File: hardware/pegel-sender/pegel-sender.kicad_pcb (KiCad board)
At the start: 2 copper layers, 100 x 70 mm, 125 parts, among them J1 SOLAR, J2 AKKU 3,2V, J3 SONDE V+ V- A B, J4 NTC extern, J5 XIAO D0-D6, J6 XIAO 5V-D7, J7 12V, Q1 AOD4189, Q10 2N7002, Q11 2N7002, Q2 FS8205A, Q3 FS8205A, Q4 AO3401A, Q5 2N7002, Q6 2N7002, Q7 SI2318CDS, Q8 2N7002, Q9 AO3401A, U1 CN3795, U10 TLV3401, U2 INA226, U3 HY2112-CB, U4 TPS63900, U5 TPS61040, U6 SC16IS740, U7 MAX3485, U8 TLV3402, U9 LM66100, Y1 14.7456MHz

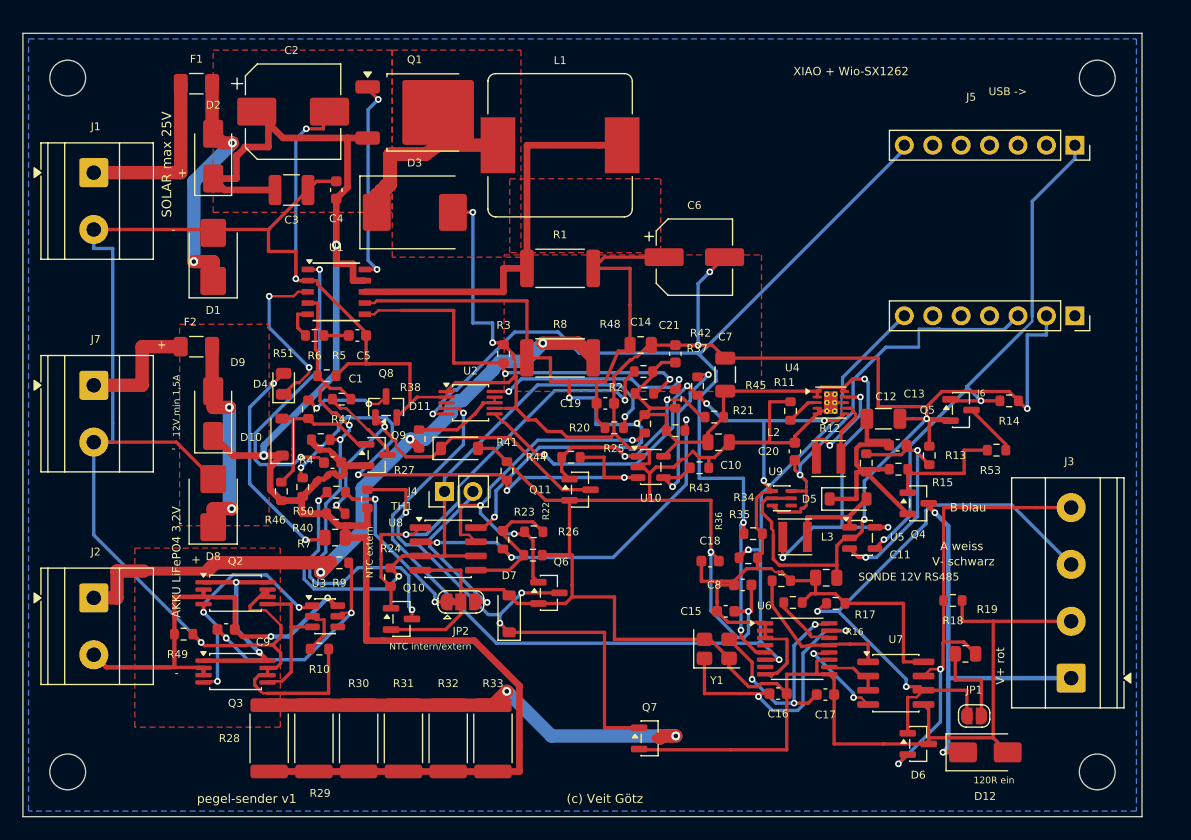
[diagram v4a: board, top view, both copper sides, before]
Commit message: hardware: circuit simulation, component stress and trace check with fixes
SPICE suite (verify/) built from design.py: 19 operating cases, sweeps,
long-term run, IPC-2221 trace check; firmware host tests with emulated
probe, SC16IS740 and INA226.

Fixes found by it: D14 blocks battery backfeed into the heater, MPPT
detection on DC_F with hysteresis, more input capacitance (C4 1210, C22),
new frost thresholds, LM2735 boost for 200 mA probe peaks, battery-low
hysteresis in firmware. Board: fixed 1.2 mm tracks L1-R1-R8, D3 and
protection FET ground vias, B.Cu keepout under the FETs.
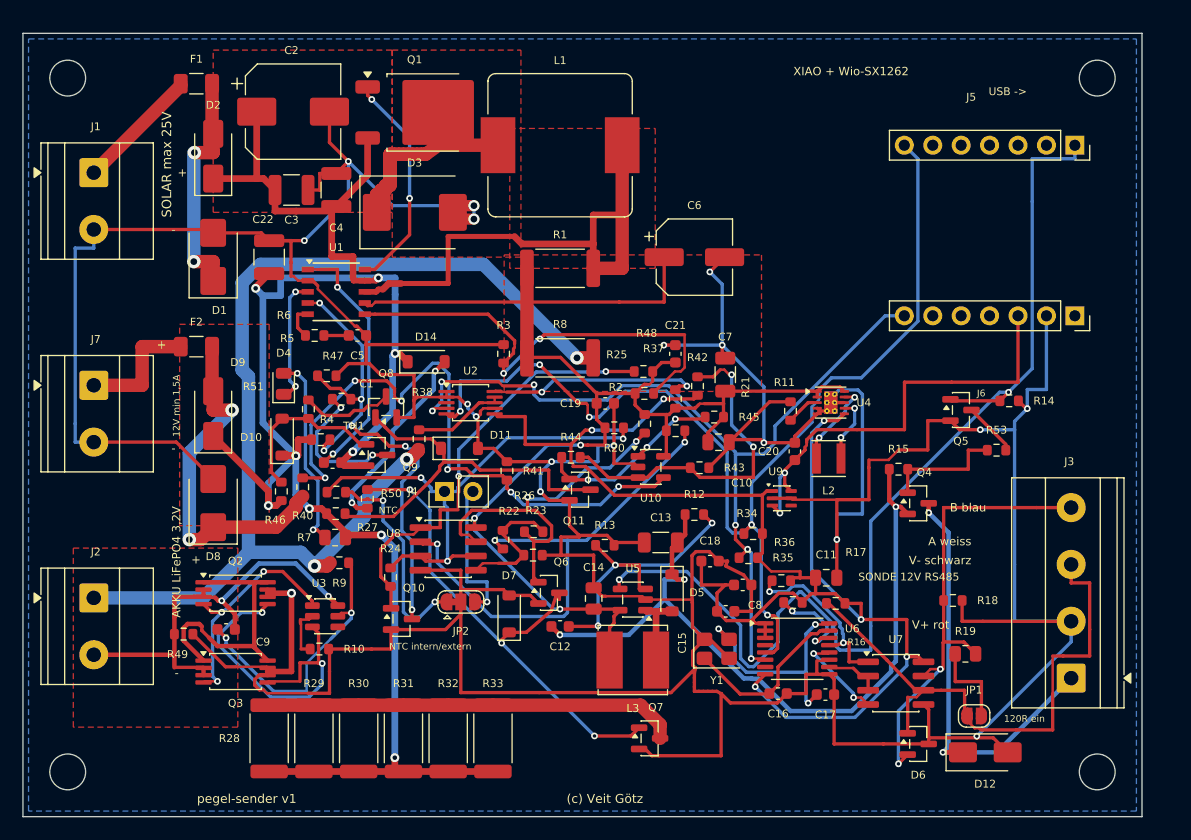
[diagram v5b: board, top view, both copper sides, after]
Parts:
- added C22: 10uF 50V, Capacitor_SMD:C_1210_3225Metric, F.Cu at (72.0, 70.0)
- added D14: 5V6, Diode_SMD:D_SOD-123, F.Cu at (86.0, 79.3)
- C1: value 100nF -> 100nF 50V
- C10: value 10uF -> 10uF 10V
- C11: value 22uF -> 22uF 6.3V
- C12: value 22pF -> 22pF 50V
- C13: value 4.7uF -> 10uF 25V
- C14: value 4.7uF -> 22uF 10V
- C15, C18, C19, C21, C8, C9: value 100nF -> 100nF 16V
- C16, C17: value 27pF -> 27pF 50V
- C20: value 1uF -> 1uF 10V
- C3: value 10uF -> 10uF 50V
- C4: value 100nF -> 10uF 50V; footprint Capacitor_SMD:C_0603_1608Metric -> Capacitor_SMD:C_1210_3225Metric
- C5: value 220nF -> 220nF 16V
- C7: value 10uF -> 10uF 16V
- J4: value NTC extern -> NTC
- L3: value 10uH -> 4.7uH; footprint Inductor_SMD:L_Taiyo-Yuden_NR-30xx -> Inductor_SMD:L_Bourns_SRN6045TA
- R1: value 40m -> 40m 2W
- R13: value 91k -> 93.1k
- R21: value 470k -> 499k
- R22: value 28.7k -> 53.6k
- R23: value 499k -> 453k
- R28, R29, R30, R31, R32, R33: value 390 -> 390 2W
- R40: value 470k -> 33k
- R41: value 68.1k -> 10k
- R8: value 10m -> 10m 2W
- U5: value TPS61040 -> LM2735
- moved C12 34.2 mm to (98.0, 103.0)
- moved R13 30.1 mm to (102.0, 95.8), turned to 0 degrees
- moved C14 23.0 mm to (101.0, 100.5), turned to 90 degrees
- moved C13 22.8 mm to (107.0, 95.5), turned to 180 degrees
- moved U5 21.2 mm to (104.5, 100.6), turned to 180 degrees
- moved L3 18.2 mm to (104.5, 106.0)
- moved D5 17.8 mm to (108.0, 100.0), turned to -90 degrees
- moved R12 16.0 mm to (110.0, 93.0), turned to 0 degrees
- turned R1 to 180 degrees
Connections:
- R27 pad 1: VSOL -> HEAT_PU
- R40 pad 1: VSOL -> DC_F
- R40 pad 2: VSOL_DIV -> DC_DIV
- R41 pad 1: VSOL_DIV -> DC_DIV
- R44 pad 2: VSOL_DIV -> MPPT_REF
- U10 pad 3: VSOL_DIV -> MPPT_REF
- U10 pad 4: MPPT_REF -> DC_DIV
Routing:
- net DC_DIV: track 0.00 -> 55.2 mm, vias 0 -> 6
- net VSOL_DIV: track 49.7 -> 0.00 mm, vias 4 -> 0
- net SENS_EN: track 49.8 -> 97.4 mm
- net V12_RAW: track 24.2 -> 68.1 mm, vias 0 -> 3
- net BAT_P: track 62.2 -> 97.8 mm
- net +3V3: track 102.0 -> 135.1 mm, vias 5 -> 6
- net VSYS: track 153.1 -> 128.1 mm, vias 6 -> 3
- net HEAT_PU: track 0.00 -> 17.6 mm, vias 0 -> 2
- net PROT_OC: track 12.6 -> 30.1 mm, vias 0 -> 2
- net CHG_CSP: track 36.1 -> 52.4 mm
- net I2C_SDA: track 92.7 -> 77.4 mm, vias 3 -> 6
- net MPPT_REF: track 16.3 -> 30.4 mm
- net DC_F: track 19.4 -> 32.5 mm
- net T_NTC: track 57.8 -> 45.7 mm
- net T_REF0: track 34.9 -> 46.2 mm
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
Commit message: hardware: larger D1, Q9 and D12; room for the J3 labels
- D1 SMBJ26A -> SMBJ28A (90 % of Vwm at -25 °C open circuit, was 97 %;
  SMBJ30A would break down above the CN3795's 33 V)
- Q9 AO3401A -> Si2319CDS (40 V, ±20 V): Uds 62 %, Ugs 50 %
- D12 SMAJ15A -> SMAJ18A: 68 % at 12.3 V
- J3: Q4, R15, R18, R19 and D12 moved; "SONDE 12V RS485" vertical
  beside the pin texts, which now sit next to their pins
- B.Cu keepout under Q2/Q3 extended to the board edge so signal
  tracks cannot fence in the GND island
- pcb_check.py evaluates zone fills on all of a zone's layers
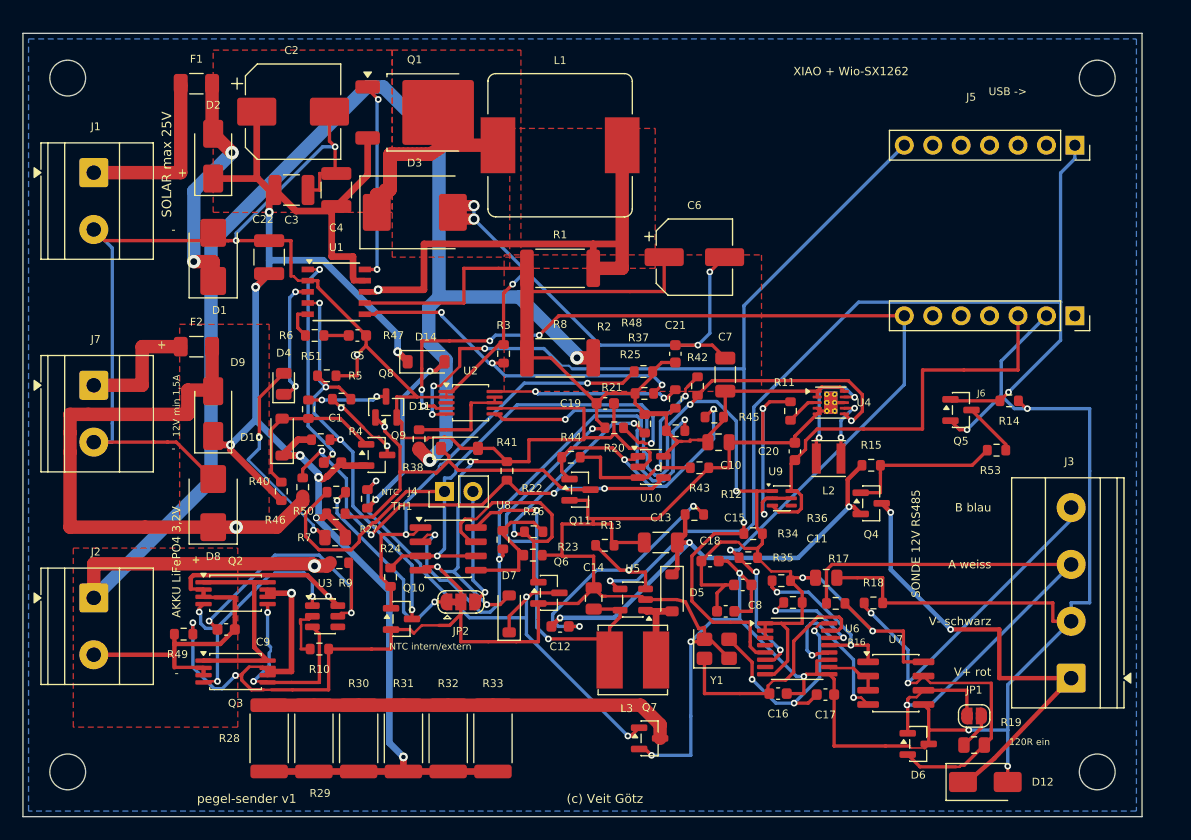
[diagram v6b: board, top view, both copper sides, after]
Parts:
- D1: value SMBJ26A -> SMBJ28A
- D12: value SMAJ15A -> SMAJ18A
- Q9: value AO3401A -> SI2319CDS
- moved R19 8.19 mm to (135.0, 113.6)
- moved R18 7.10 mm to (126.0, 100.9)
- moved Q4 4.20 mm to (125.8, 92.0)
- moved D12 2.65 mm to (136.0, 116.9)
- moved R15 2.46 mm to (125.8, 88.6)
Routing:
- net BAT_P: track 97.8 -> 136.3 mm
- net V12_RAW: track 68.1 -> 44.7 mm
- net GND: track 546.2 -> 564.9 mm, vias 18 -> 24
- net DC_F: track 32.5 -> 51.2 mm, vias 2 -> 1
- net T_NTC: track 45.7 -> 63.1 mm, vias 3 -> 2
- net I2C_SDA: track 77.4 -> 92.8 mm, vias 6 -> 7
- net DC_DIV: track 55.2 -> 41.7 mm, vias 6 -> 4
- net VSYS: track 128.1 -> 141.6 mm
- net +3V3: track 135.1 -> 123.6 mm
- net PROT_OC: track 30.1 -> 18.8 mm
- net CHG_FB: track 42.0 -> 31.6 mm, vias 2 -> 3
- net RS485_B: track 42.3 -> 52.4 mm
- net SENS_EN: track 97.4 -> 87.9 mm
- net MPPT_REF: track 30.4 -> 21.6 mm
- net VSOL: track 166.3 -> 157.8 mm, vias 9 -> 8
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
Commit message: hardware: cheapest JLCPCB build, basic/preferred parts only
All 45 SMD part types are JLCPCB basic or preferred (no loading fee);
inductors, terminals and XIAO sockets are through-hole for hand soldering.

- Charger: TPS5430 buck at 3.50 V; LM324 limits current to 2 A (shunt in
  the battery minus), holds the panel near 17 V (proportional loop, the
  integrator oscillated in weak light) and handles frost lock and heater.
  Single input for solar or 12 V supply, header jumper NETZTEIL.
- XIAO runs from the battery through a Schottky diode; no 3.3 V regulator,
  no INA226, no protection IC (firmware measures VDD, sleeps below 2.6 V).
- RS485: SP3485 on Serial1 with automatic direction, powered with the
  probe; no SC16IS740, no termination resistor.
- Probe 12 V from TPS61040 (30 mA).
- NTC and heater resistor at the battery via J4.
- New compact placement, 45 degree corners, wider traces and clearances,
  JLCPCB BOM/CPL export, user README, technical README for the board.
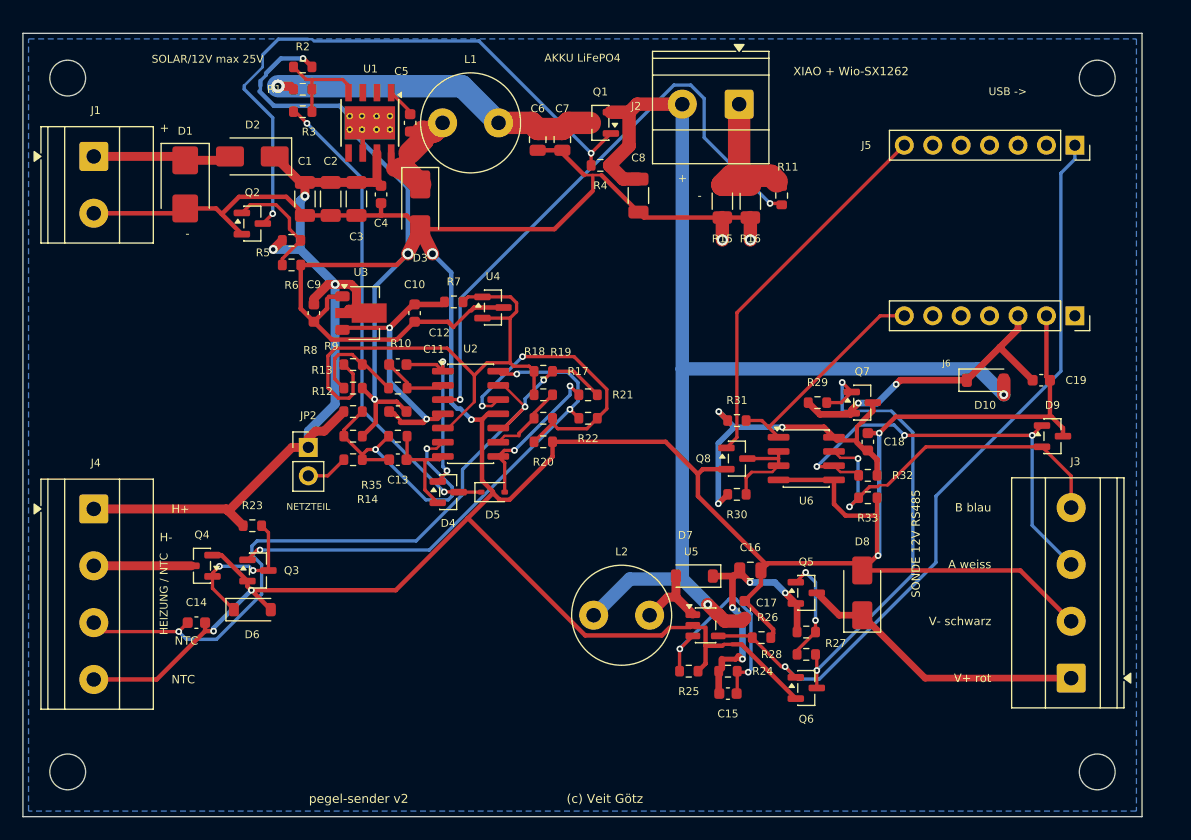
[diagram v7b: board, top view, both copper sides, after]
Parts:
- removed C20: 1uF 10V, Capacitor_SMD:C_0603_1608Metric
- removed C21: 100nF 16V, Capacitor_SMD:C_0603_1608Metric
- removed C22: 10uF 50V, Capacitor_SMD:C_1210_3225Metric
- removed D11: 10V, Diode_SMD:D_SOD-123
- removed D12: SMAJ18A, Diode_SMD:D_SMA
- removed D14: 5V6, Diode_SMD:D_SOD-123
- removed F1, F2: 2A, Fuse:Fuse_1206_3216Metric
- removed J7: 12V, TerminalBlock_Phoenix:TerminalBlock_Phoenix_MKDS-1,5-2-5.08_1x02_P5.08mm_Horizontal
- removed JP1: 120R ein, Jumper:SolderJumper-2_P1.3mm_Open_RoundedPad1.0x1.5mm
- removed L3: 4.7uH, Inductor_SMD:L_Bourns_SRN6045TA
- removed Q10, Q11: 2N7002, Package_TO_SOT_SMD:SOT-23
- removed Q9: SI2319CDS, Package_TO_SOT_SMD:SOT-23
- removed R34: 4.7k, Resistor_SMD:R_0603_1608Metric
- removed R36, R41, R51: 10k, Resistor_SMD:R_0603_1608Metric
- removed R37, R38: 10, Resistor_SMD:R_0603_1608Metric
- removed R40: 33k, Resistor_SMD:R_0603_1608Metric
- removed R42: 976k, Resistor_SMD:R_0603_1608Metric
- removed R43, R44, R45, R48, R50: 1M, Resistor_SMD:R_0603_1608Metric
- removed R46, R49, R53: 100k, Resistor_SMD:R_0603_1608Metric
- removed R47: 330k, Resistor_SMD:R_0603_1608Metric
- removed TH1: 100k B4250, Resistor_SMD:R_0603_1608Metric
- removed U10: TLV3401, Package_TO_SOT_SMD:SOT-23-5
- removed U7: MAX3485, Package_SO:SOIC-8_3.9x4.9mm_P1.27mm
- removed U8: TLV3402, Package_SO:SOIC-8_3.9x4.9mm_P1.27mm
- removed U9: LM66100, Package_TO_SOT_SMD:SOT-363_SC-70-6
- removed Y1: 14.7456MHz, Crystal:Crystal_SMD_3225-4Pin_3.2x2.5mm
- C1: value 100nF 50V -> 10uF 50V; footprint Capacitor_SMD:C_0603_1608Metric -> Capacitor_SMD:C_1206_3216Metric
- C10: value 10uF 10V -> 1uF; footprint Capacitor_SMD:C_0805_2012Metric -> Capacitor_SMD:C_0603_1608Metric
- C11: value 22uF 6.3V -> 100nF; footprint Capacitor_SMD:C_0805_2012Metric -> Capacitor_SMD:C_0603_1608Metric
- C12: value 22pF 50V -> 100nF
- C13: value 10uF 25V -> 100pF; footprint Capacitor_SMD:C_1206_3216Metric -> Capacitor_SMD:C_0603_1608Metric
- C14: value 22uF 10V -> 100nF; footprint Capacitor_SMD:C_0805_2012Metric -> Capacitor_SMD:C_0603_1608Metric
- C15: value 100nF 16V -> 22pF
- C16: value 27pF 50V -> 10uF 25V; footprint Capacitor_SMD:C_0603_1608Metric -> Capacitor_SMD:C_0805_2012Metric
- C17: value 27pF 50V -> 10uF 10V
- C18: value 100nF 16V -> 100nF
- C19: value 100nF 16V -> 10uF 10V
- C2: value 100uF 35V -> 10uF 50V; footprint Capacitor_SMD:CP_Elec_8x10 -> Capacitor_SMD:C_1206_3216Metric
- C3: footprint Capacitor_SMD:C_1210_3225Metric -> Capacitor_SMD:C_1206_3216Metric
- C4: value 10uF 50V -> 100nF; footprint Capacitor_SMD:C_1210_3225Metric -> Capacitor_SMD:C_0603_1608Metric
- C5: value 220nF 16V -> 10nF
- C6: value 100uF 10V -> 22uF 25V; footprint Capacitor_SMD:CP_Elec_6.3x7.7 -> Capacitor_SMD:C_0805_2012Metric
- C7: value 10uF 16V -> 22uF 25V; footprint Capacitor_SMD:C_1206_3216Metric -> Capacitor_SMD:C_0805_2012Metric
- C8: value 100nF 16V -> 100uF 6.3V; footprint Capacitor_SMD:C_0603_1608Metric -> Capacitor_SMD:C_1206_3216Metric
- C9: value 100nF 16V -> 1uF
- D10: value 10V -> B5819W
- D2: value SS34 -> SS54
- D3: value B540C -> SS54; footprint Diode_SMD:D_SMC -> Diode_SMD:D_SMA
- D4: value rot -> BAV70; footprint LED_SMD:LED_0805_2012Metric -> Package_TO_SOT_SMD:SOT-23
- D5: value MBR0540 -> 1N4148WS; footprint Diode_SMD:D_SOD-123 -> Diode_SMD:D_SOD-323
- D6: value SM712 -> 10V; footprint Package_TO_SOT_SMD:SOT-23 -> Diode_SMD:D_SOD-123
- D7: value 12V -> B0540W
- D8: value SMBJ18A -> SMAJ18A; footprint Diode_SMD:D_SMB -> Diode_SMD:D_SMA
- D9: value SS34 -> PSM712; footprint Diode_SMD:D_SMA -> Package_TO_SOT_SMD:SOT-23
- J1: value SOLAR -> SOLAR / 12V
- J4: value NTC -> HEIZ NTC; footprint Connector_PinHeader_2.54mm:PinHeader_1x02_P2.54mm_Vertical -> TerminalBlock_Phoenix:TerminalBlock_Phoenix_MKDS-1,5-4-5.08_1x04_P5.08mm_Horizontal
- JP2: value NTC intern/extern -> NETZTEIL; footprint Jumper:SolderJumper-3_P1.3mm_Bridged12_RoundedPad1.0x1.5mm -> Connector_PinHeader_2.54mm:PinHeader_1x02_P2.54mm_Vertical
- L1: footprint Inductor_SMD:L_Bourns_SRP1245A -> Inductor_THT:L_Radial_D8.7mm_P5.00mm_Fastron_07HCP
- L2: value 2.2uH -> 10uH; footprint Inductor_SMD:L_Taiyo-Yuden_NR-30xx -> Inductor_THT:L_Radial_D8.7mm_P5.00mm_Fastron_07HCP
- Q1: value AOD4189 -> AO3401A; footprint Package_TO_SOT_SMD:TO-252-2 -> Package_TO_SOT_SMD:SOT-23
- Q2, Q3: value FS8205A -> 2N7002; footprint Package_SO:TSSOP-8_4.4x3mm_P0.65mm -> Package_TO_SOT_SMD:SOT-23
- Q4: value AO3401A -> HL2310A
- Q5: value 2N7002 -> AO3401A
- Q7: value SI2318CDS -> AO3401A
- R1: value 40m 2W -> 56k; footprint Resistor_SMD:R_2512_6332Metric -> Resistor_SMD:R_0603_1608Metric
- R10: value 2k -> 10k
- R11: value 36.5k -> 1k
- R12: value 820k -> 300k
- R13: value 93.1k -> 51k
- R14: value 100k -> 300k
- R15: value 100k -> 0.1; footprint Resistor_SMD:R_0603_1608Metric -> Resistor_SMD:R_1206_3216Metric
- R16: value 10k -> 0.1; footprint Resistor_SMD:R_0603_1608Metric -> Resistor_SMD:R_1206_3216Metric
- R17: value 10k -> 27k
- R18: value 10k -> 47k
- R19: value 120 -> 5.1k; footprint Resistor_SMD:R_0805_2012Metric -> Resistor_SMD:R_0603_1608Metric
- R2: value 200k -> 30k
- R20: value 330k -> 49.9k
- R21: value 499k -> 1M
- R22: value 53.6k -> 2M
- R23: value 453k -> 100k
- R24: value 4.7M -> 510k
- R25: value 1M -> 56k
- R26: value 10M -> 100k
- R28, R29, R31: value 390 2W -> 100k; footprint Resistor_SMD:R_2512_6332Metric -> Resistor_SMD:R_0603_1608Metric
- R3: value 100k -> 10k
- R30, R32, R33: value 390 2W -> 10k; footprint Resistor_SMD:R_2512_6332Metric -> Resistor_SMD:R_0603_1608Metric
- R35: value 4.7k -> 1M
- R4: value 300k -> 100k
- R5: value 21.5k -> 100k
- R6: value 120 -> 47k
- R7: value 10k -> 2.2k; footprint Resistor_SMD:R_0805_2012Metric -> Resistor_SMD:R_0603_1608Metric
- R8: value 10m 2W -> 24k; footprint Resistor_SMD:R_2512_6332Metric -> Resistor_SMD:R_0603_1608Metric
- R9: value 330 -> 1k
- U1: value CN3795 -> TPS5430; footprint Package_SO:SSOP-10_3.9x4.9mm_P1.00mm -> Package_SO:TI_SO-PowerPAD-8_ThermalVias
- U2: value INA226 -> LM324; footprint Package_SO:TSSOP-10_3x3mm_P0.5mm -> Package_SO:SOIC-14_3.9x8.7mm_P1.27mm
- U3: value HY2112-CB -> HT7550-1; footprint Package_TO_SOT_SMD:SOT-23-6 -> Package_TO_SOT_SMD:SOT-89-3
- U4: value TPS63900 -> CJ431; footprint Package_SON:WSON-10-1EP_2.5x2.5mm_P0.5mm_EP1.2x2mm_ThermalVias -> Package_TO_SOT_SMD:SOT-23
- U5: value LM2735 -> TPS61040
- U6: value SC16IS740 -> SP3485EN; footprint Package_SO:TSSOP-16_4.4x5mm_P0.65mm -> Package_SO:SOIC-8_3.9x4.9mm_P1.27mm
- moved D9 75.0 mm to (142.0, 86.0), turned to 0 degrees
- moved J2 72.6 mm to (114.0, 56.3), turned to 180 degrees
- moved D10 63.0 mm to (136.0, 81.0), turned to 0 degrees
- moved D6 60.7 mm to (70.5, 101.5)
- moved Q4 60.1 mm to (66.0, 97.6), turned to 180 degrees
- moved R14 58.9 mm to (79.5, 88.1)
- moved D8 58.6 mm to (125.0, 100.0)
- moved R29 54.1 mm to (121.0, 83.0), turned to 0 degrees
- moved R28 48.6 mm to (120.0, 105.5), turned to 0 degrees
- moved R19 48.3 mm to (96.5, 84.4)
- moved R32 44.3 mm to (125.5, 89.5), turned to 0 degrees
- moved R2 42.2 mm to (75.0, 53.0)
- moved R31 41.2 mm to (113.8, 84.6), turned to 0 degrees
- moved C11 41.1 mm to (83.5, 83.8)
- moved R27 41.0 mm to (120.0, 103.5), turned to 0 degrees
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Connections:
- C1 pad 1: CHG_VG -> VSOL
- C1 pad 2: VSOL -> GND
- C10 pad 1: VSYS -> +5V
- C11 pad 1: +3V3 -> +5V
- C12 pad 1: V12_RAW -> CC_INT
- C12 pad 2: BST_FB -> CC_OUT
- C13 pad 1: V12_RAW -> VIN_DIV
- C13 pad 2: GND -> VIN_OUT
- C14 pad 1: VSYS -> T_NTC
- C15 pad 1: +3V3 -> V12_RAW
- C15 pad 2: GND -> BST_FB
- C16 pad 1: XTAL1 -> V12_RAW
- C17 pad 1: XTAL2 -> VSYS
- C18 pad 1: +3V3 -> RS_VCC
- C19 pad 1: VSYS -> XIAO_3V3
- C5 pad 1: CHG_COMC -> CHG_BOOT
- C5 pad 2: GND -> CHG_SW
- C6 pad 1: VSYS -> CHG_OUT
- C7 pad 1: VSYS -> CHG_OUT
- C8 pad 1: +3V3 -> VSYS
- C9 pad 1: PROT_VDD -> VSOL
- C9 pad 2: BAT_N -> GND
- D1 pad 1: SOLAR_F -> IN_RAW
- D10 pad 1: VSOL -> XIAO_3V3
- D10 pad 2: MPPT_GATE -> VSYS
- D2 pad 2: SOLAR_F -> IN_RAW
- D4 pad 1: CHG_LED -> CC_OUT
- D4 pad 2: CHG_LEDA -> VIN_OUT
- D5 pad 1: V12_RAW -> CHG_LIM
- D5 pad 2: BST_SW -> CHG_INH
- D6 pad 1: RS485_A -> HEAT_G
- D6 pad 2: RS485_B -> GND
- D7 pad 1: HEAT_G -> V12_RAW
- D7 pad 2: GND -> BST_SW
- D8 pad 1: DC_F -> V12_PROBE
- D9 pad 1: VSOL -> RS485_A
- D9 pad 2: DC_F -> RS485_B
- J1 pad 1: SOLAR_RAW -> IN_RAW
- J2 pad 1: BAT_P -> BAT_N
- J2 pad 2: BAT_N -> VSYS
- J4 pad 1: T_NTC -> VSOL
- J4 pad 2: NTC_SEL3 -> HEAT_N
- J5 pad 7: I2C_SCL -> UART_TX
- J6 pad 7: I2C_SDA -> UART_RX
- JP2 pad 1: NTC_SEL1 -> VSOL
- JP2 pad 2: GND -> VIN_J
- L1 pad 2: CHG_CSP -> CHG_OUT
- L2 pad 1: BB_LX1 -> VSYS
- L2 pad 2: BB_LX2 -> BST_SW
- Q1 pad 1: CHG_DRV -> CHG_PG
- Q1 pad 2: CHG_SW -> VSYS
- Q1 pad 3: VSOL -> CHG_OUT
- Q2 pad 1: PROT_D -> CHG_PGD
- Q2 pad 2: BAT_N -> GND
- Q2 pad 3: BAT_N -> CHG_PG
- Q3 pad 1: PROT_D -> HEAT_OFF
- Q3 pad 2: BAT_N -> GND
- Q3 pad 3: BAT_N -> HEAT_G
- Q4 pad 1: PSW_G -> HEAT_G
- Q4 pad 2: V12_RAW -> GND
- Q4 pad 3: V12_PROBE -> HEAT_N
- Q5 pad 1: SENS_EN -> PSW_G
- Q5 pad 2: GND -> V12_RAW
- Q5 pad 3: PSW_PD -> V12_PROBE
- Q6 pad 1: HEAT_OFF -> SENS_EN
- Q6 pad 3: HEAT_G -> PSW_PD
- Q7 pad 1: HEAT_G -> PSW_PD
- Q7 pad 2: GND -> XIAO_3V3
- Q7 pad 3: HEAT_N -> RS_VCC
- Q8 pad 1: MPPT_NG -> UART_TX
- Q8 pad 3: MPPT_PD -> RS_DE
- R1 pad 1: CHG_CSP -> CHG_OUT
- R1 pad 2: VSYS -> CHG_FB
- R10 pad 1: PROT_CS -> CC_SET
- R10 pad 2: GND -> CC_INT
- R11 pad 1: BB_CFG1 -> BAT_N
- R11 pad 2: GND -> CC_SENSE
- R12 pad 1: V12_RAW -> VSOL
- R12 pad 2: BST_FB -> VIN_DIV
- R13 pad 1: BST_FB -> VIN_DIV
- R14 pad 1: SENS_EN -> VIN_J
- R14 pad 2: GND -> VIN_DIV
- R15 pad 1: V12_RAW -> BAT_N
- R15 pad 2: PSW_G -> GND
- R16 pad 1: UART_RST -> BAT_N
- R16 pad 2: +3V3 -> GND
- R17 pad 1: RS485_A -> VREF
- R17 pad 2: +3V3 -> T_NTC
- R18 pad 1: RS485_B -> VREF
- R18 pad 2: GND -> T_REF0
- R19 pad 1: RS485_TERM -> T_REF0
- R19 pad 2: RS485_B -> T_REF2
- R2 pad 1: VSYS -> CHG_FB
- R2 pad 2: CHG_FB -> GND
- R20 pad 1: VSYS -> T_REF2
- R20 pad 2: T_NTC -> GND
- R21 pad 1: VSYS -> CHG_INH
- R21 pad 2: T_REF0 -> T_NTC
- R22 pad 1: T_REF0 -> HEAT_OFF
- R23 pad 1: T_REF2 -> VSOL
- R23 pad 2: GND -> HEAT_G
- R24 pad 1: CHG_INHIBIT -> V12_RAW
- R24 pad 2: T_NTC -> BST_FB
- R25 pad 1: HEAT_OFF -> BST_FB
- R25 pad 2: VSYS -> GND
- R26 pad 1: HEAT_OFF -> SENS_EN
- R26 pad 2: T_REF2 -> GND
- R27 pad 1: HEAT_PU -> V12_RAW
- R27 pad 2: HEAT_G -> PSW_G
- R28 pad 1: VSOL -> PSW_G
- R28 pad 2: HEAT_N -> PSW_PD
- R29 pad 1: VSOL -> XIAO_3V3
- R29 pad 2: HEAT_N -> PSW_PD
- R3 pad 1: CHG_FB -> CHG_LIM
- R3 pad 2: GND -> CHG_FB
- R30 pad 1: VSOL -> RS_VCC
- R30 pad 2: HEAT_N -> RS_DE
- R31 pad 1: VSOL -> RS_VCC
- R31 pad 2: HEAT_N -> UART_RX
- R32 pad 1: VSOL -> RS485_A
- R32 pad 2: HEAT_N -> RS_VCC
- R33 pad 1: VSOL -> RS485_B
- R33 pad 2: HEAT_N -> GND
- R35 pad 1: I2C_SDA -> VIN_DIV
- R35 pad 2: +3V3 -> VIN_OUT
- R4 pad 1: VSOL -> CHG_PG
- R4 pad 2: MPPT -> VSYS
- R5 pad 1: MPPT -> VSOL
- R5 pad 2: GND -> CHG_PGD
- R6 pad 1: CHG_COM -> CHG_PGD
- R6 pad 2: CHG_COMC -> GND
- R7 pad 1: CHG_LEDA -> +5V
- R7 pad 2: VSOL -> VREF
- R8 pad 1: VSYS -> VREF
- R8 pad 2: BAT_P -> CC_SET
- R9 pad 1: BAT_P -> CC_SET
- R9 pad 2: PROT_VDD -> GND
- U1 pad 1: CHG_VG -> CHG_BOOT
- U1 pad 2: GND -> (no net)
- U1 pad 3: CHG_LED -> (no net)
- U1 pad 4: MPPT -> CHG_FB
- U1 pad 5: CHG_COM -> (no net)
- U1 pad 6: CHG_FB -> GND
- U1 pad 7: VSYS -> VSOL
- U1 pad 8: CHG_CSP -> CHG_SW
- U1 pad 9: VSOL -> GND
- U2 pad 1: GND -> CC_OUT
- U2 pad 10: INA_P -> T_NTC
- U2 pad 2: GND -> CC_INT
- U2 pad 3: (no net) -> CC_SENSE
- U2 pad 4: I2C_SDA -> +5V
- U2 pad 5: I2C_SCL -> VREF
- U2 pad 6: +3V3 -> VIN_DIV
- U2 pad 7: GND -> VIN_OUT
- U2 pad 8: INA_M -> CHG_INH
- U2 pad 9: INA_M -> T_REF0
- U3 pad 1: PROT_OD -> GND
- U3 pad 2: PROT_CS -> VSOL
- U3 pad 3: PROT_OC -> +5V
- U4 pad 1: VSYS -> VREF
- U4 pad 2: VSYS -> VREF
- U4 pad 3: BB_CFG1 -> GND
- U6 pad 1: +3V3 -> UART_RX
- U6 pad 2: +3V3 -> RS_DE
- U6 pad 3: +3V3 -> RS_DE
- U6 pad 4: (no net) -> GND
- U6 pad 5: I2C_SCL -> GND
- U6 pad 6: I2C_SDA -> RS485_A
- U6 pad 7: (no net) -> RS485_B
- U6 pad 8: +3V3 -> RS_VCC
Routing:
- net BAT_P: track 136.3 -> 0.00 mm, vias 3 -> 0
- net GND: track 564.9 -> 434.7 mm, vias 24 -> 11
- net +3V3: track 123.6 -> 0.00 mm, vias 6 -> 0
- net I2C_SCL: track 94.6 -> 0.00 mm, vias 4 -> 0
- net I2C_SDA: track 92.8 -> 0.00 mm, vias 7 -> 0
- net VSOL: track 157.8 -> 79.4 mm, vias 8 -> 3
- net CHG_PG: track 0.00 -> 54.9 mm, vias 0 -> 2
- net CC_SENSE: track 0.00 -> 53.7 mm, vias 0 -> 2
- net CHG_CSP: track 51.5 -> 0.00 mm, vias 1 -> 0
- net DC_F: track 51.2 -> 0.00 mm, vias 1 -> 0
- net VREF: track 0.00 -> 50.6 mm
- net T_REF0: track 53.1 -> 7.00 mm, vias 3 -> 0
- net CHG_LIM: track 0.00 -> 43.0 mm, vias 0 -> 2
- net DC_DIV: track 41.7 -> 0.00 mm, vias 4 -> 0
- net CHG_INHIBIT: track 39.0 -> 0.00 mm, vias 2 -> 0
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- removed copper zone on F.Cu, net BAT_N
- removed copper zone on F.Cu, net CHG_CSP
- removed copper zone on F.Cu, net CHG_SW
- removed copper zone on F.Cu, net DC_F
- removed copper zone on F.Cu, net VSOL
- removed copper zone on F.Cu, net VSYS
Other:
- board text added: "AKKU LiFePO4"
- board text added: "H+"
- board text added: "H-"
- board text added: "HEIZUNG / NTC"
- board text added: "NTC"
- board text added: "SOLAR/12V max 25V"
- board text added: "pegel-sender v2"
- board text removed: "12V min 1,5A"
- board text removed: "AKKU LiFePO4 3,2V"
- board text removed: "SOLAR max 25V"
- board text removed: "pegel-sender v1"
